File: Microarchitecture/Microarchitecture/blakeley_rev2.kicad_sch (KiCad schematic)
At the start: 15 parts

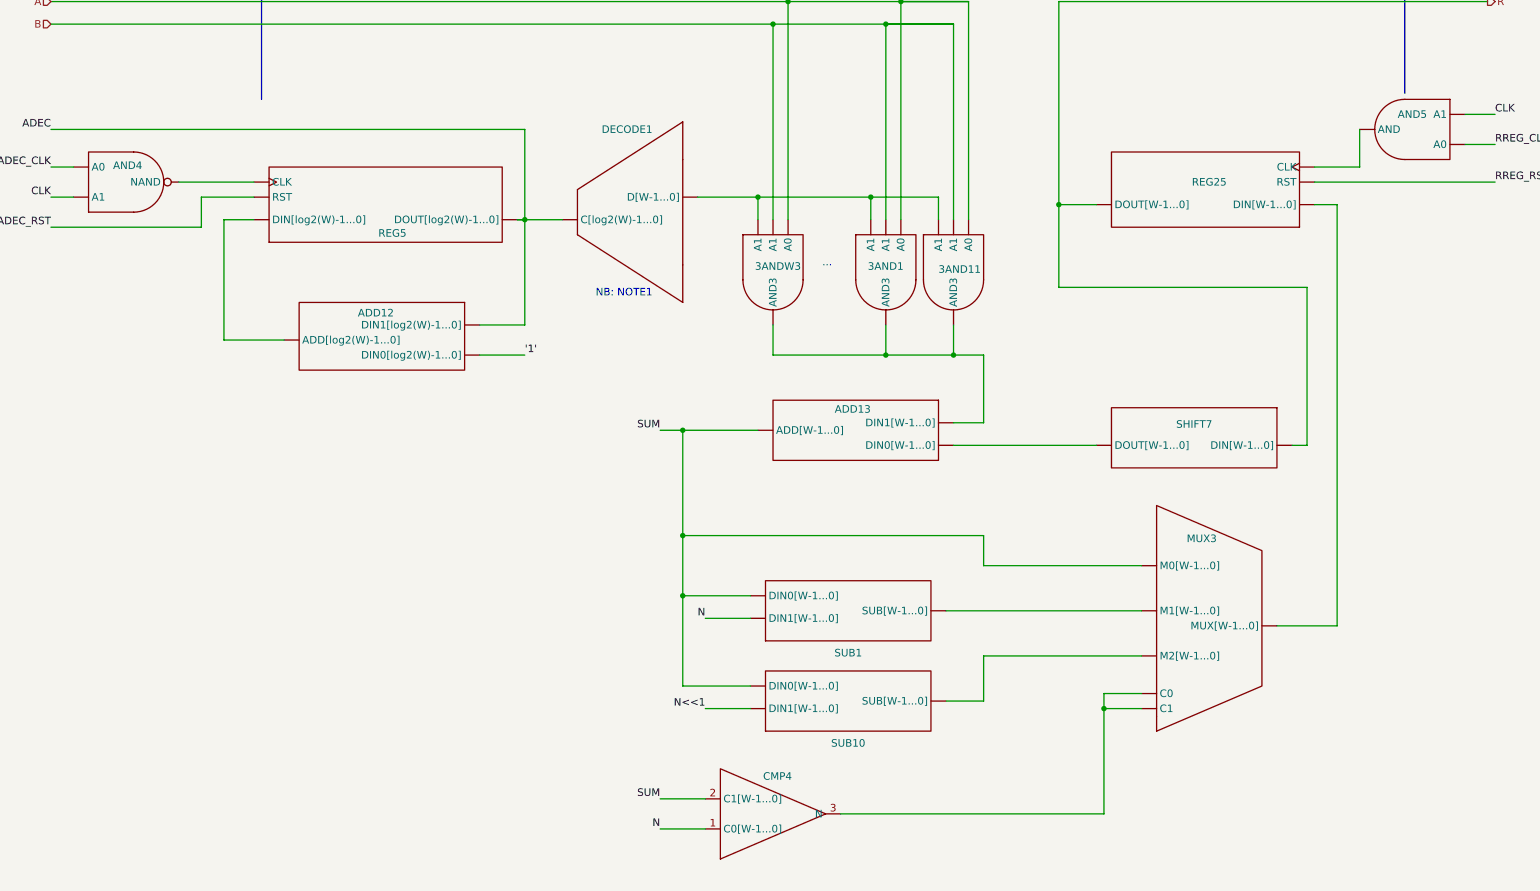
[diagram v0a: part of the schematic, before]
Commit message: Blakeley datapath working
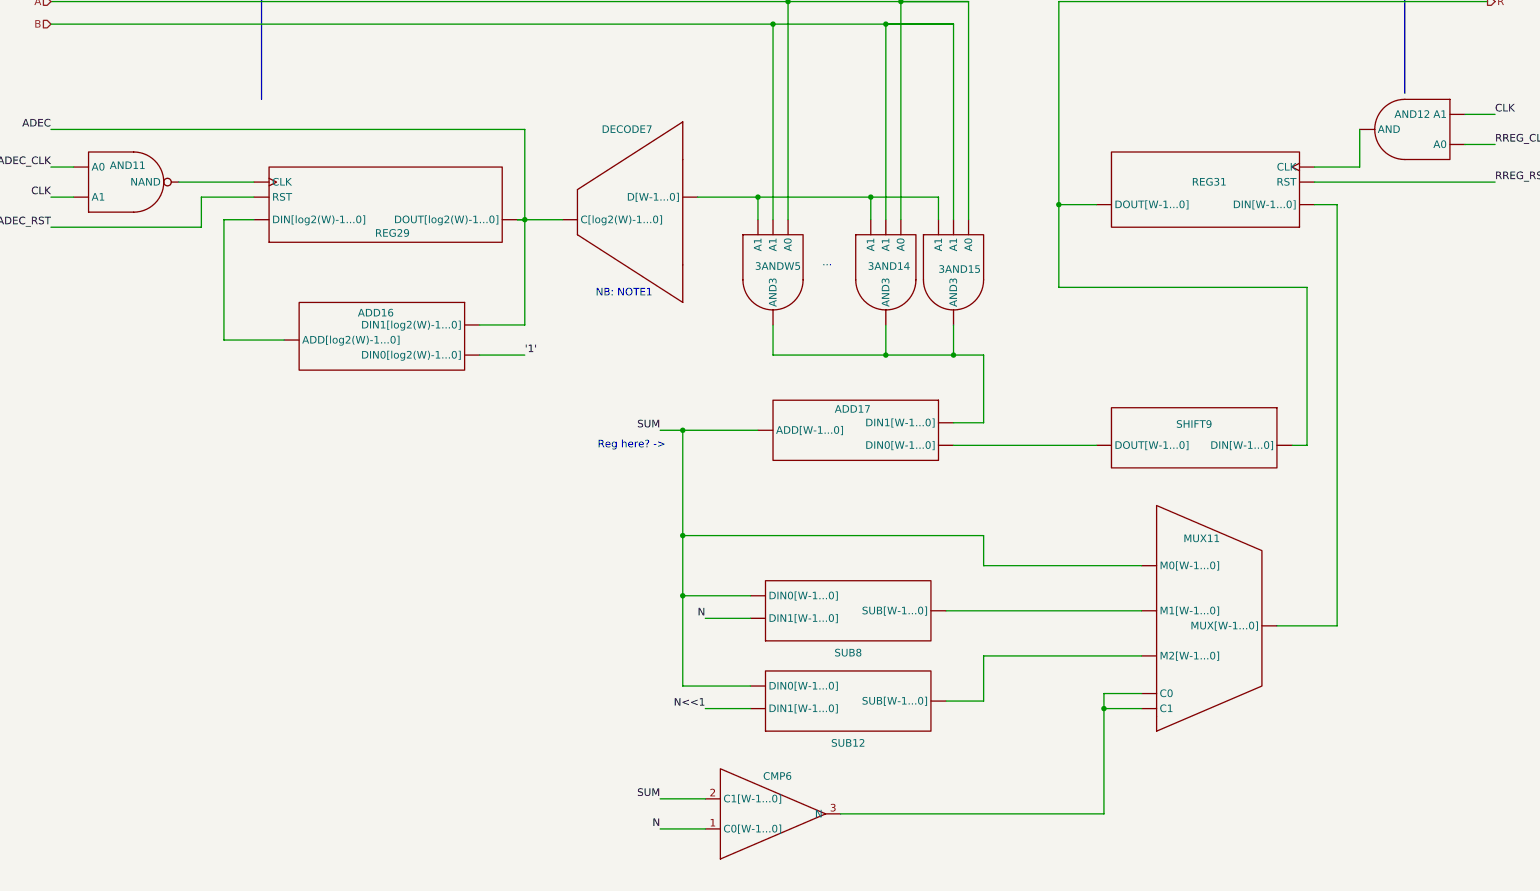
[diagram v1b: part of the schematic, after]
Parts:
- renumbered 3AND1 to 3AND14, 3AND11 to 3AND15, 3ANDW3 to 3ANDW5, ADD12 to ADD16, ADD13 to ADD17, AND4 to AND11, AND5 to AND12, CMP4 to CMP6, DECODE1 to DECODE7, MUX3 to MUX11, REG5 to REG29, REG25 to REG31, SHIFT7 to SHIFT9, SUB10 to SUB12, SUB1 to SUB8
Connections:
- new net: MUX11. (MUX[W-1...0]), SUB12. (SUB[W-1...0])
- new net: AND12. (AND), REG31. (RST)
- new net: MUX11. (MUX[W-1...0]), REG31. (RST)
- new net: 3AND14. (AND3), 3AND15. (AND3), 3ANDW5. (AND3), ADD17. (DIN1[W-1...0])
- new net: 3AND14. (AND3), 3AND15. (AND3), 3ANDW5. (AND3), DECODE7. (D[W-1...0])
- new net: MUX11. (MUX[W-1...0]), SUB8. (SUB[W-1...0])
- new net: ADD17. (DIN1[W-1...0]), SHIFT9. (DOUT[W-1...0])
- new net: AND11. (NAND), REG29. (RST)
- new net: ADD16. (DIN1[log2(W)-1...0]), REG29. (RST)
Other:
- note added: "Reg here? ->"
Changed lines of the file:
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@@
+		)
+	)
+	(text "Reg here? ->"
+		(exclude_from_sim no)
+		(at 217.424 133.35 0)
+		(effects
+			(font
+				(size 1.27 1.27)
+			)
 		)
 	)
@@
 		(on_board yes)
 		(dnp no)
-		(property "Reference" "SUB10"
+		(property "Reference" "SUB12"
 			(at 254 183.642 0)
 			(effects
@@
 		(on_board yes)
 		(dnp no)
-		(property "Reference" "AND5"
+		(property "Reference" "AND12"
 			(at 349.25 77.47 90)
 			(effects
@@
 	)
 	(symbol
-		(lib_name "Symbols:REG")
 		(lib_id "Symbols:REG")
 		(at 320.04 90.17 180)
@@
 		(on_board yes)
 		(dnp no)
-		(property "Reference" "REG25"
+		(property "Reference" "REG31"
 			(at 314.96 88.9 0)
 			(effects
@@
 	)
 	(symbol
-		(lib_name "Symbols:AND3")
 		(lib_id "Symbols:AND3")
 		(at 241.3 102.87 0)
@@
 		(on_board yes)
 		(dnp no)
-		(property "Reference" "3ANDW3"
+		(property "Reference" "3ANDW5"
 			(at 238.252 103.124 0)
 			(effects
@@
 		(on_board yes)
 		(dnp no)
-		(property "Reference" "SUB1"
+		(property "Reference" "SUB8"
 			(at 254 168.402 0)
 			(effects
@@
 	)
 	(symbol
-		(lib_name "Symbols:ADD")
 		(lib_id "Symbols:ADD")
 		(at 251.46 123.19 0)
@@
 		(on_board yes)
 		(dnp no)
-		(property "Reference" "ADD13"
+		(property "Reference" "ADD17"
 			(at 254.762 127.254 0)
 			(effects
@@
 		(on_board yes)
 		(dnp no)
-		(property "Reference" "MUX3"
+		(property "Reference" "MUX11"
 			(at 313.69 149.098 0)
 			(effects
@@
 	)
 	(symbol
-		(lib_name "Symbols:AND3")
 		(lib_id "Symbols:AND3")
 		(at 260.35 102.87 0)
@@
 		(on_board yes)
 		(dnp no)
-		(property "Reference" "3AND1"
+		(property "Reference" "3AND14"
 			(at 257.302 103.124 0)
 			(effects
@@
 		(on_board yes)
 		(dnp no)
-		(property "Reference" "REG5"
+		(property "Reference" "REG29"
 			(at 177.038 97.536 0)
 			(effects
@@
 		(on_board yes)
 		(dnp no)
-		(property "Reference" "DECODE1"
+		(property "Reference" "DECODE7"
 			(at 216.662 80.01 0)
 			(effects
@@
 		(on_board yes)
 		(dnp no)
-		(property "Reference" "AND4"
+		(property "Reference" "AND11"
 			(at 132.334 86.106 90)
 			(effects
@@
 		(on_board yes)
 		(dnp no)
-		(property "Reference" "CMP4"
+		(property "Reference" "CMP6"
 			(at 242.062 189.23 0)
 			(effects
@@
 		(on_board yes)
 		(dnp no)
-		(property "Reference" "ADD12"
+		(property "Reference" "ADD16"
 			(at 174.244 110.998 0)
 			(effects
@@
 		(on_board yes)
 		(dnp no)
-		(property "Reference" "SHIFT7"
+		(property "Reference" "SHIFT9"
 			(at 312.42 129.794 0)
 			(effects
@@
 	)
 	(symbol
-		(lib_name "Symbols:AND3")
 		(lib_id "Symbols:AND3")
 		(at 271.78 102.87 0)
@@
 		(on_board yes)
 		(dnp no)
-		(property "Reference" "3AND11"
+		(property "Reference" "3AND15"
 			(at 269.24 103.632 0)
 			(effects

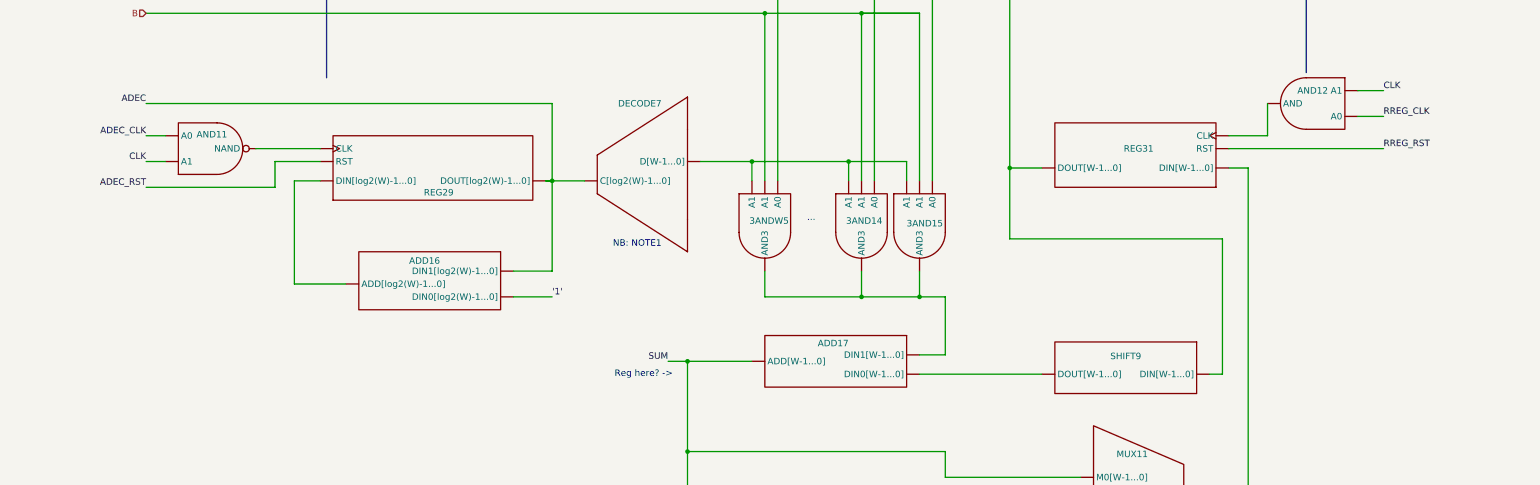
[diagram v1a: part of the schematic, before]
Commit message: TB for blakeley module ok, discovered datapath add logic error
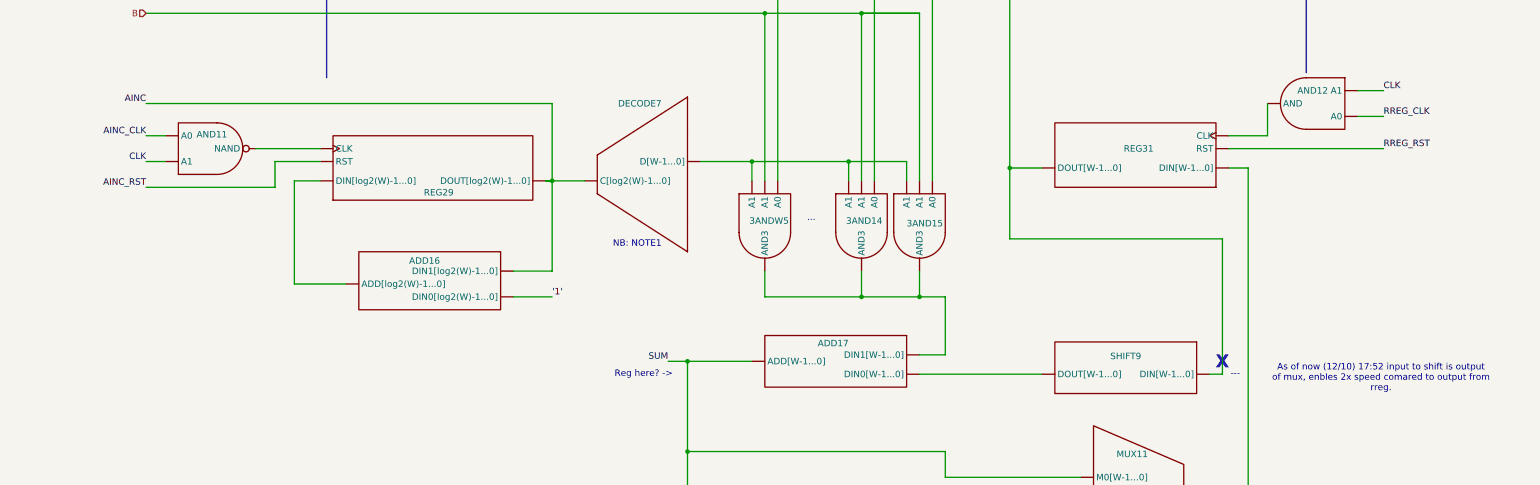
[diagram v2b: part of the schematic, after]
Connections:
- net ADEC_CLK is gone; now on net CLK: AND11. (NAND)
- net ADEC_RST is gone; now on net AINC_RST: REG29. (RST)
- net AINC_RST: now reaches REG29. (RST)
- net AINC_RST: no longer AND11. (NAND)
- net AINC: now reaches ADD16. (DIN1[log2(W)-1...0]), REG29. (RST)
- net AINC: now also DECODE7. (D[W-1...0])
- removed net ADEC: ADD16. (DIN1[log2(W)-1...0]), DECODE7. (D[W-1...0]), REG29. (RST)
- new net: MUX11. (MUX[W-1...0]), SUB12. (SUB[W-1...0])
- new net: AND12. (AND), REG31. (RST)
- new net: MUX11. (MUX[W-1...0]), REG31. (RST)
- new net: 3AND14. (AND3), 3AND15. (AND3), 3ANDW5. (AND3), ADD17. (DIN1[W-1...0])
- new net: 3AND14. (AND3), 3AND15. (AND3), 3ANDW5. (AND3), DECODE7. (D[W-1...0])
- new net: MUX11. (MUX[W-1...0]), SUB8. (SUB[W-1...0])
- new net: ADD17. (DIN1[W-1...0]), SHIFT9. (DOUT[W-1...0])
- new net: AND11. (NAND), REG29. (RST)
- new net: ADD16. (DIN1[log2(W)-1...0]), REG29. (RST)
- new net AINC_CLK: AND11. (NAND)
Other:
- note added: "---"
- note added: "As of now (12/10) 17:52 input to shift is output of mux, enbles 2x speed comared to output from rreg."
- note added: "X"
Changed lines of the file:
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@@
+		)
+	)
+	(text "As of now (12/10) 17:52 input to shift is output\nof mux, enbles 2x speed comared to output from\nrreg."
+		(exclude_from_sim no)
+		(at 362.712 134.112 0)
+		(effects
+			(font
+				(size 1.27 1.27)
+			)
+		)
+	)
+	(text "X"
+		(exclude_from_sim no)
+		(at 331.47 131.064 0)
+		(effects
+			(font
+				(size 2.54 2.54)
+				(thickness 0.508)
+				(bold yes)
+			)
 		)
 	)
@@
 		(exclude_from_sim no)
 		(at 251.714 42.926 0)
+		(effects
+			(font
+				(size 1.27 1.27)
+			)
+		)
+	)
+	(text "---"
+		(exclude_from_sim no)
+		(at 334.01 133.35 0)
 		(effects
 			(font
@@
 		)
 	)
-	(label "ADEC_RST"
+	(label "AINC_RST"
 		(at 119.38 96.52 180)
 		(fields_autoplaced yes)
@@
 		)
 	)
-	(label "ADEC"
+	(label "AINC"
 		(at 119.38 80.01 180)
 		(fields_autoplaced yes)
@@
 		)
 	)
-	(label "ADEC_CLK"
+	(label "AINC_CLK"
 		(at 119.38 86.36 180)
 		(fields_autoplaced yes)

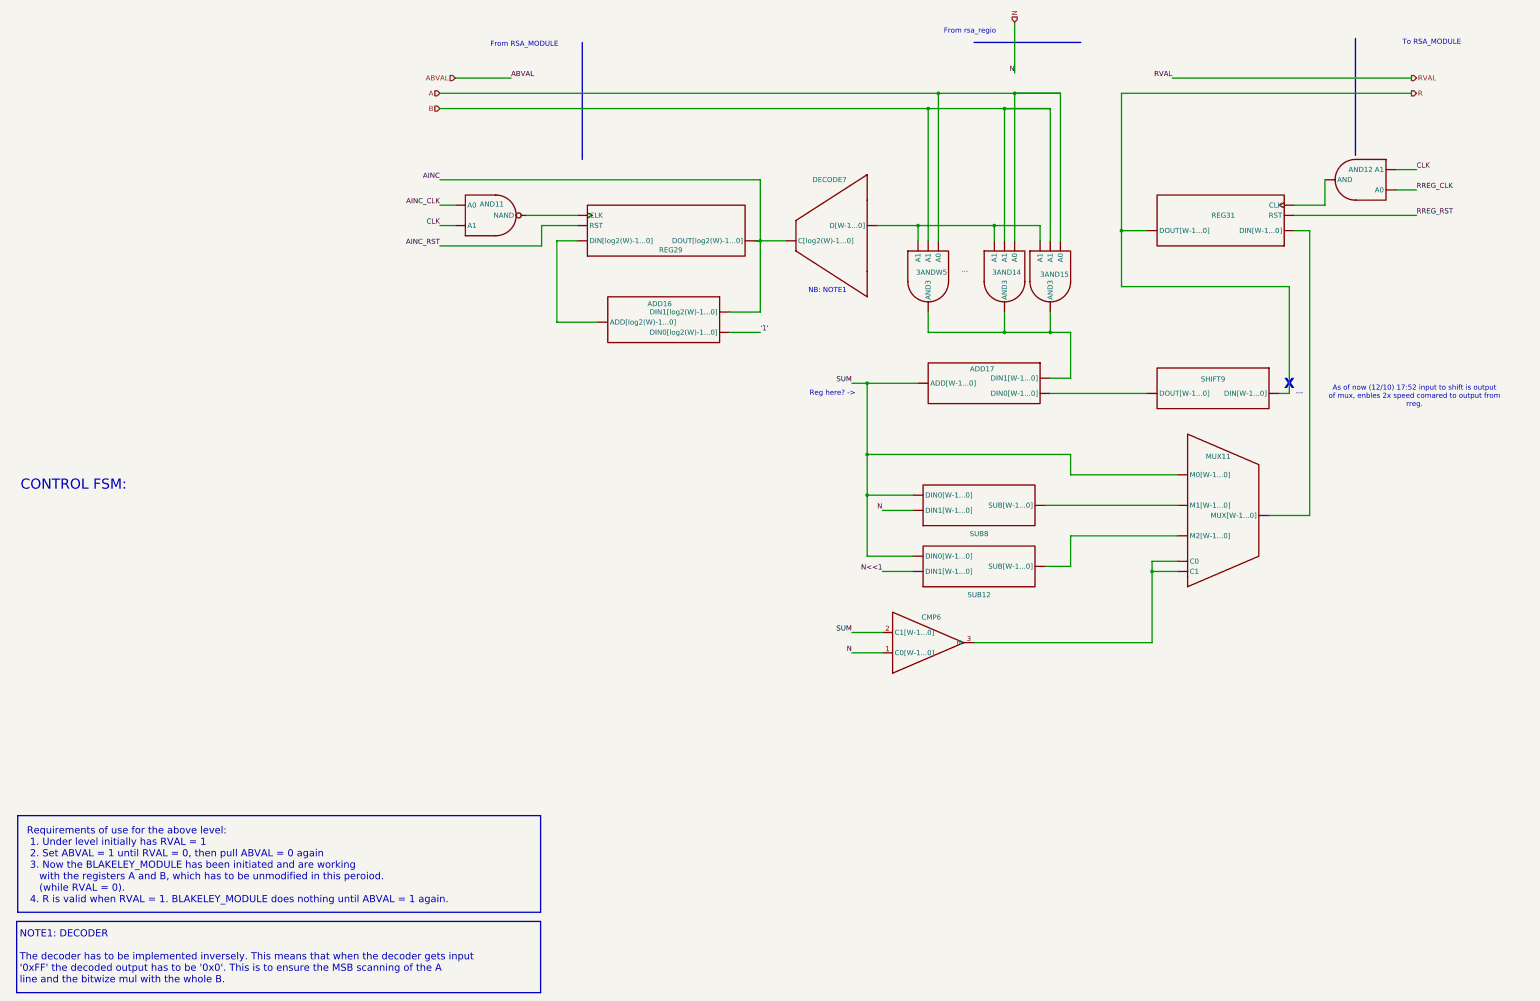
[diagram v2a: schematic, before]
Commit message: Removed debugging layouts
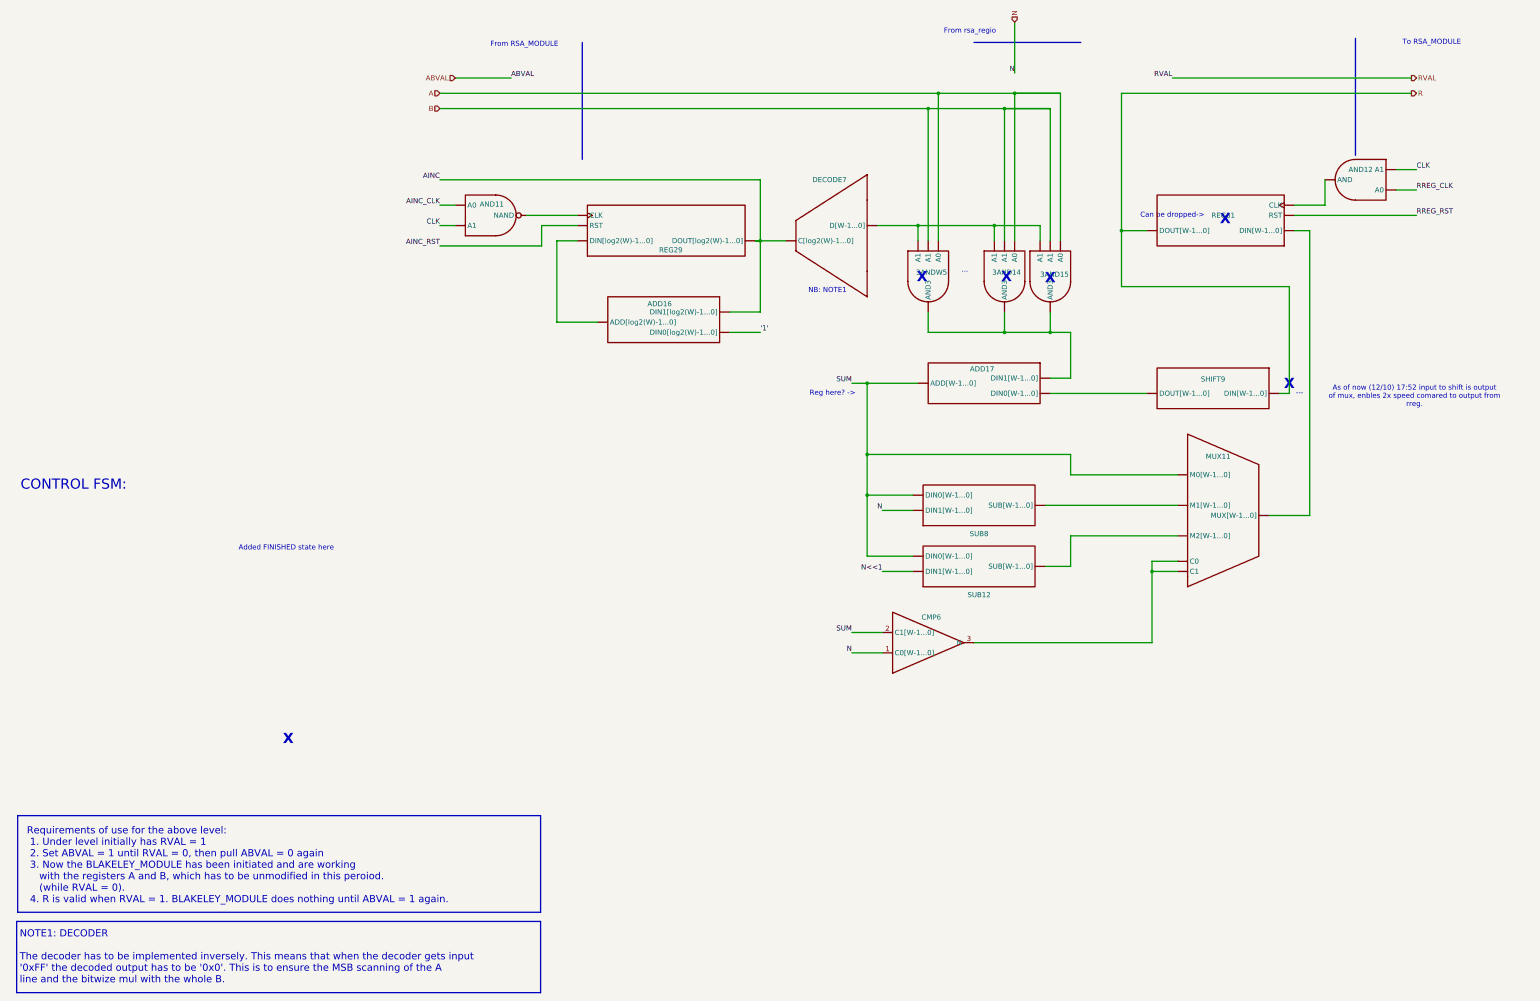
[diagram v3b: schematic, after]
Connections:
- new net: MUX11. (MUX[W-1...0]), SUB12. (SUB[W-1...0])
- new net: AND12. (AND), REG31. (RST)
- new net: MUX11. (MUX[W-1...0]), REG31. (RST)
- new net: 3AND14. (AND3), 3AND15. (AND3), 3ANDW5. (AND3), ADD17. (DIN1[W-1...0])
- new net: 3AND14. (AND3), 3AND15. (AND3), 3ANDW5. (AND3), DECODE7. (D[W-1...0])
- new net: MUX11. (MUX[W-1...0]), SUB8. (SUB[W-1...0])
- new net: ADD17. (DIN1[W-1...0]), SHIFT9. (DOUT[W-1...0])
- new net: AND11. (NAND), REG29. (RST)
- new net: ADD16. (DIN1[log2(W)-1...0]), REG29. (RST)
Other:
- note added: "Added FINISHED state here"
- note added: "Can be dropped->"
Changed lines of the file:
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@@
+		)
+	)
+	(text "X"
+		(exclude_from_sim no)
+		(at 81.534 219.71 0)
+		(effects
+			(font
+				(size 2.54 2.54)
+				(thickness 0.508)
+				(bold yes)
+			)
 		)
 	)
@@
 		(exclude_from_sim no)
 		(at 362.712 134.112 0)
+		(effects
+			(font
+				(size 1.27 1.27)
+			)
+		)
+	)
+	(text "Added FINISHED state here"
+		(exclude_from_sim no)
+		(at 81.026 171.958 0)
 		(effects
 			(font
@@
 		)
 	)
+	(text "X"
+		(exclude_from_sim no)
+		(at 315.468 89.916 0)
+		(effects
+			(font
+				(size 2.54 2.54)
+				(thickness 0.508)
+				(bold yes)
+			)
+		)
+	)
+	(text "X"
+		(exclude_from_sim no)
+		(at 260.858 104.394 0)
+		(effects
+			(font
+				(size 2.54 2.54)
+				(thickness 0.508)
+				(bold yes)
+			)
+		)
+	)
+	(text "X"
+		(exclude_from_sim no)
+		(at 239.776 104.394 0)
+		(effects
+			(font
+				(size 2.54 2.54)
+				(thickness 0.508)
+				(bold yes)
+			)
+		)
+	)
 	(text "NOTE1: DECODER\n\nThe decoder has to be implemented inversely. This means that when the decoder gets input\n'0xFF' the decoded output has to be '0x0'. This is to ensure the MSB scanning of the A\nline and the bitwize mul with the whole B. "
 		(exclude_from_sim no)
@@
 			)
 			(justify left)
+		)
+	)
+	(text "Can be dropped->\n"
+		(exclude_from_sim no)
+		(at 302.26 88.9 0)
+		(effects
+			(font
+				(size 1.27 1.27)
+			)
 		)
 	)
@@
 			)
 		)
+	)
+	(text "X"
+		(exclude_from_sim no)
+		(at 271.78 104.648 0)
+		(effects
+			(font
+				(size 2.54 2.54)
+				(thickness 0.508)
+				(bold yes)
+			)
+		)
